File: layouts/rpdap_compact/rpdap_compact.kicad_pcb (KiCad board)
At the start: 4 copper layers, 35.8 x 38.2 mm, 62 parts

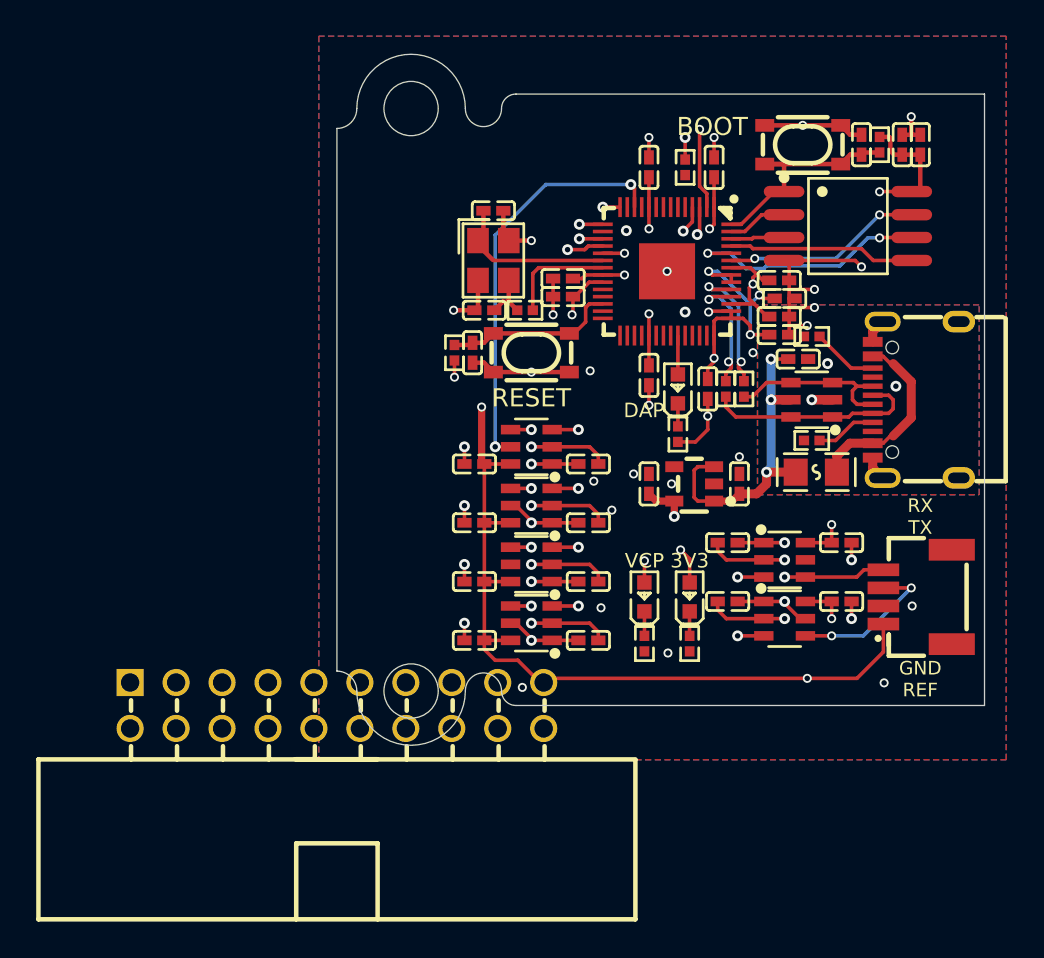
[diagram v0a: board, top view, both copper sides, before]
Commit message: refactor debug-connectors, fix issues in layout and connections
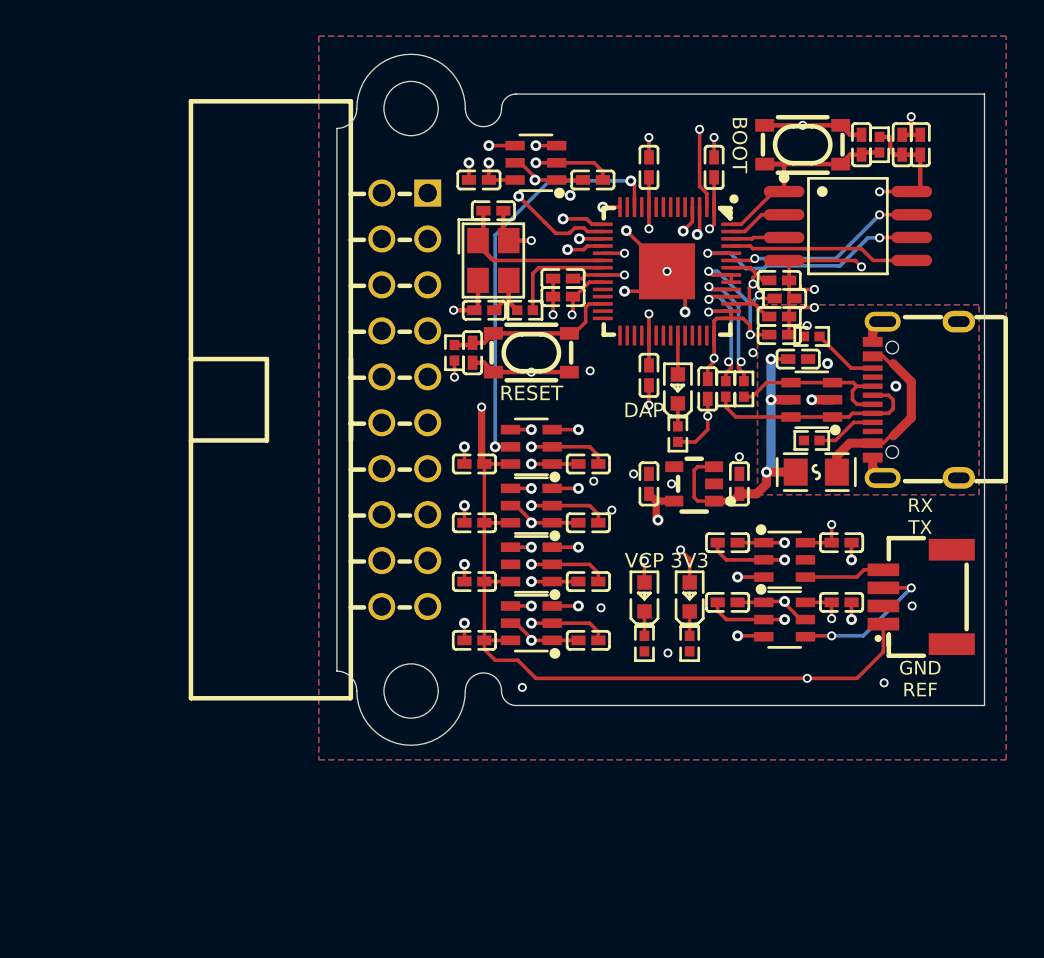
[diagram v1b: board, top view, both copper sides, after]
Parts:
- removed R11: 10kΩ ±1% 62.5mW, UNI_ROYAL_0402WGF1002TCE:R0402
- added C32: 100nF ±10% 16V X7R, Samsung_Electro_Mechanics_CL05B104KO5NNNC:C0402, F.Cu at (21.6, -9.00)
- added C33: 100nF ±10% 16V X7R, Samsung_Electro_Mechanics_CL05B104KO5NNNC:C0402, F.Cu at (27.9, -9.00)
- added U1: , Wuxi_I_core_Elec_AiP74LVC1T45GB236_TR:SOT-23-6_L2.9-W1.6-P0.95-LS2.8-BL, F.Cu at (24.8, -8.05)
- R2: value 100kΩ ±1% 62.5mW -> 10kΩ ±1% 62.5mW; footprint UNI_ROYAL_0402WGF1003TCE:R0402 -> UNI_ROYAL_0402WGF1002TCE:R0402
- moved C12 30.7 mm to (7.85, -29.1), turned to 180 degrees
- moved U7 28.7 mm to (11.0, -30.0), turned to 90 degrees
- moved R2 26.4 mm to (17.0, -3.42), turned to -90 degrees
- moved C11 24.5 mm to (14.2, -29.1), turned to 0 degrees
- moved J1 17.3 mm to (3.75, -16.9), turned to -90 degrees
- moved C14 3.30 mm to (27.9, -5.70)
- moved U8 3.30 mm to (24.8, -4.75)
- moved C13 3.30 mm to (21.6, -5.70)
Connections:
- net DI renamed data_0
- net DO renamed data_1
- net QSPI_SD2 renamed data_2
- net QSPI_SD3 renamed data_3
- net _11 renamed return_test_clock-line
- net _17 renamed DBGRQ
- net _3 renamed N_TRST
- net analog[1]-line renamed gpio[27]-line
- net gpio[11]-line renamed model-a-line-1
- net level_shifter[0]-a-line renamed model-a-line-0
- net level_shifter[2]-a-line renamed model-a-line-2
- net level_shifter[3]-a-line renamed model-a-line-3
- net power_indicator-cathode renamed footprint-cathode-0
- net rpdap-net renamed footprint-net
- net usb_connector-net renamed connector-net
- C1 pad 1: VBUS -> _power_vbus-VCC
- C10 pad 1: 3V3 -> reference-VCC
- C12 pad 1: 3V3 -> reference-VCC
- C14 pad 1: 3V3 -> reference-VCC
- C31 pad 1: VBUS -> _power_vbus-VCC
- C4 pad 1: 3V3 -> reference-VCC
- C6 pad 1: 3V3 -> reference-VCC
- C8 pad 1: 3V3 -> reference-VCC
- CN1 pad 1: 3V3 -> reference-VCC
- CN1 pad 3: TARGET_UART_TX -> uart-TX
- CN1 pad 4: TARGET_UART_RX -> uart-RX
- D1 pad 5: VBUS -> _power_vbus-VCC
- F1 pad 2: VBUS -> _power_vbus-VCC
- J1 pad 1: _1 -> reference-VCC
- J1 pad 10: _10 -> GND
- J1 pad 12: _12 -> GND
- J1 pad 13: _13 -> TDO_SWO
- J1 pad 15: _15 -> nRESET
- J1 pad 19: _19 -> _power_vbus-VCC
- J1 pad 4: _4 -> GND
- J1 pad 5: _5 -> TDI
- J1 pad 6: _6 -> GND
- J1 pad 7: _7 -> TMS_DIO
- J1 pad 8: _8 -> GND
- J1 pad 9: _9 -> TCK_SWCLK
- LED3 pad 1: vcp_indicator-cathode -> footprint-cathode-1
- R2 pad 1: TARGET_GND_DETECT -> footprint-cathode-1
- R2 pad 2: 3V3 -> GND
- U2 pad 1: VBUS -> _power_vbus-VCC
- U2 pad 3: VBUS -> _power_vbus-VCC
- U3 pad 4: TARGET_SWDIO -> TMS_DIO
- U3 pad 6: 3V3 -> reference-VCC
- U4 pad 4: TARGET_SWCLK -> TCK_SWCLK
- U4 pad 5: (no net) -> 3V3
- U4 pad 6: 3V3 -> reference-VCC
- U5 pad 4: TARGET_SWO -> TDO_SWO
- U5 pad 5: GND -> (no net)
- U5 pad 6: 3V3 -> reference-VCC
- U6 pad 4: TARGET_RESET -> nRESET
- U6 pad 5: (no net) -> 3V3
- U6 pad 6: 3V3 -> reference-VCC
- U7 pad 3: TX -> model-a-line-4
- U7 pad 4: TARGET_UART_TX -> TDI
- U7 pad 5: (no net) -> 3V3
- U7 pad 6: 3V3 -> reference-VCC
- U8 pad 3: RX -> a-TX
- U8 pad 4: TARGET_UART_RX -> uart-TX
- U8 pad 5: GND -> 3V3
- U8 pad 6: 3V3 -> reference-VCC
- U9 pad 16: GPIO13 -> model-a-line-4
- U9 pad 2: TX -> a-TX
- U9 pad 3: RX -> a-RX
- U9 pad 5: TARGET_GND_DETECT -> SCL
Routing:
- net (no net): track 135.4 -> 0.00 mm, vias 24 -> 0
- net reference-VCC: track 0.00 -> 77.3 mm, vias 0 -> 5
- net 3V3: track 0.00 -> 66.1 mm, vias 0 -> 20
- net VBUS: track 43.8 -> 0.00 mm, vias 3 -> 0
- net _power_vbus-VCC: track 0.00 -> 43.8 mm, vias 0 -> 3
- net a-TX: track 0.00 -> 37.9 mm, vias 0 -> 2
- net TX: track 37.9 -> 0.00 mm, vias 2 -> 0
- net RX: track 22.9 -> 0.00 mm, vias 2 -> 0
- net a-RX: track 0.00 -> 22.9 mm, vias 0 -> 2
- net GND: track 77.5 -> 91.5 mm, vias 45 -> 49
- net TDI: track 0.00 -> 11.0 mm, vias 0 -> 1
- net TCK_SWCLK: track 0.00 -> 10.7 mm, vias 0 -> 1
- net TARGET_SWCLK: track 10.7 -> 0.00 mm, vias 1 -> 0
- net model-a-line-4: track 0.00 -> 10.4 mm, vias 0 -> 2
- net TMS_DIO: track 0.00 -> 10.2 mm, vias 0 -> 1
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- added copper zone on In1.Cu, net 3V3
- removed copper zone on In1.Cu, net (none)

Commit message: rebuild, small fixes, update README
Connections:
- U1 pad 5: (no net) -> GND
- U5 pad 5: (no net) -> GND
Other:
- outline, holes or cut-outs redrawn
- board text added: "RPDAP"
- board text added: "compact"
- board text added: "{{GITHASH}}"

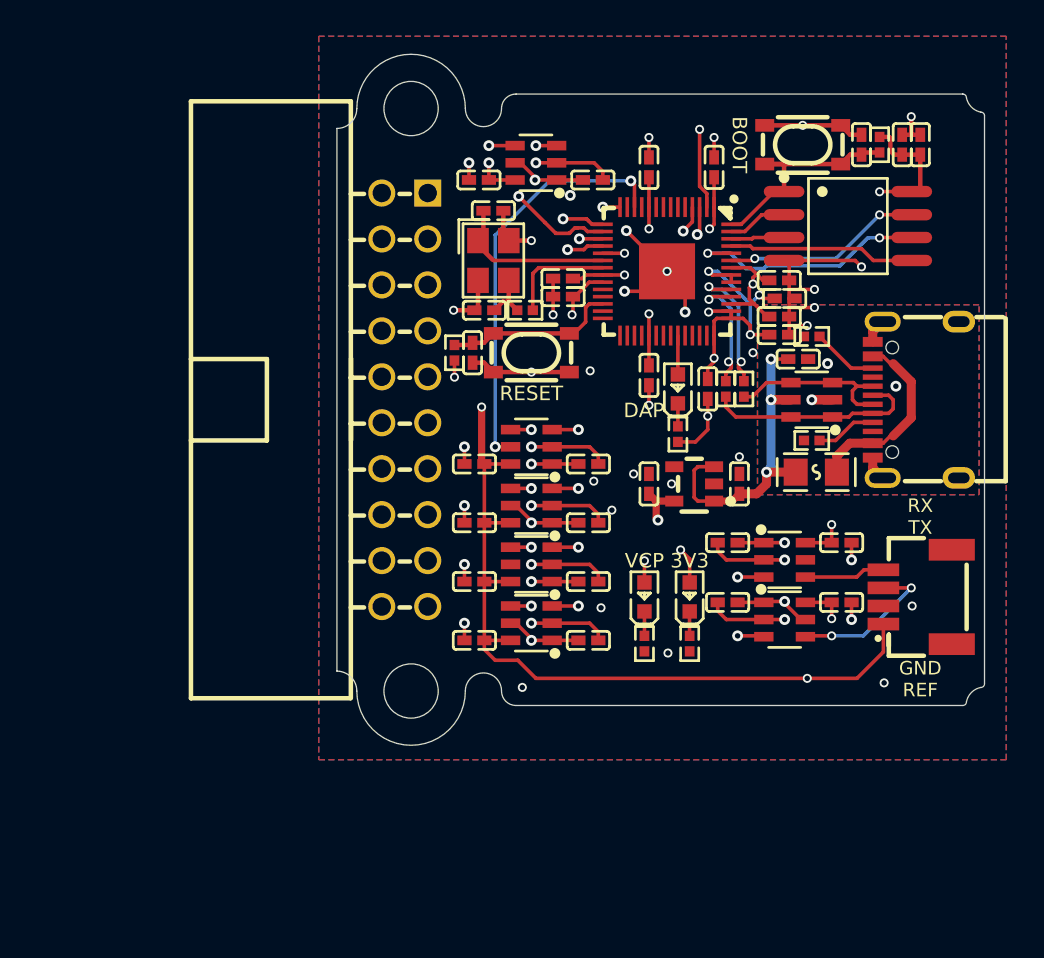
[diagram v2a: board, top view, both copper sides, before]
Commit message: rebuild with upstream rp2040 fixes. move header .25mm to the right. center dap-LED
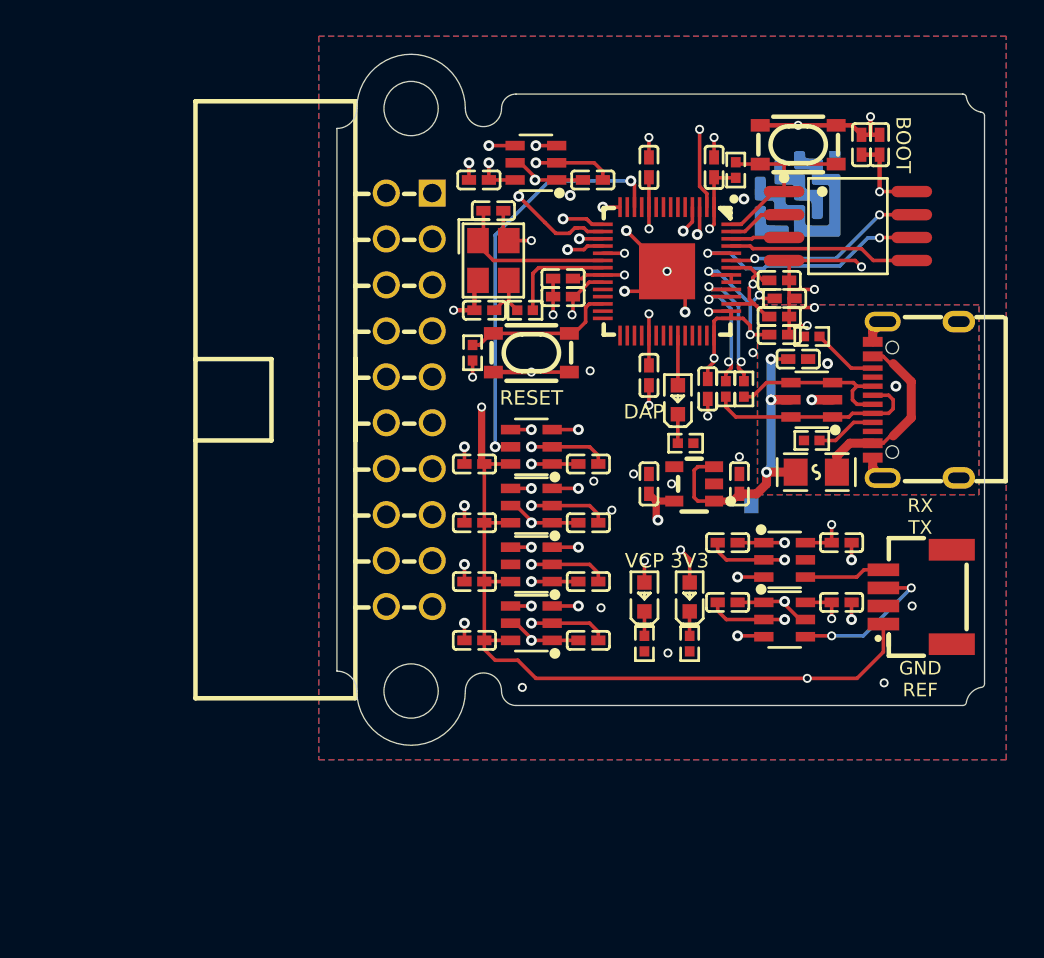
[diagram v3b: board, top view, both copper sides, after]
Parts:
- removed C15, C30: 1µF ±10% 25V X5R, Samsung_Electro_Mechanics_CL05A105KA5NQNC:C0402
- added LOGO1: , atopile_Logo_25x6mm:atopile_Logo_25x6mm, B.Cu at (25.5, -18.0)
- X1: footprint Yangxing_Tech_X322512MSB4SI:CRYSTAL-SMD_4P-L3.2-W2.5-BL -> Abracon_LLC_ABM8_272_T3:CRYSTAL-SMD_4P-L3.2-W2.5-BL
- moved R3 8.07 mm to (22.1, -29.6)
- moved C29 2.25 mm to (29.0, -31.0)
- moved C28 2.25 mm to (30.0, -31.0)
- moved R6 1.00 mm to (7.50, -19.5), turned to -90 degrees
- moved R5 0.66 mm to (19.3, -14.5), turned to 180 degrees
- moved LED2 0.60 mm to (18.9, -16.9)
- moved J1 0.25 mm to (4.00, -16.9)
- moved SW1 0.25 mm to (25.5, -31.0), turned to 180 degrees
- turned SW2 to 0 degrees
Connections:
- net RP_USB_N renamed output-USB_D_N
- net RP_USB_P renamed output-USB_D_P
- net USB_N renamed input-USB_D_N
- net USB_P renamed input-USB_D_P
- net _power_vbus-VCC renamed Vbus_fused
- R3 pad 1: 3V3 -> chip_select
- R3 pad 2: chip_select -> 3V3
- R6 pad 1: 3V3 -> RUN
- R6 pad 2: RUN -> 3V3
- SW1 pad 1: GND -> chip_select
- SW1 pad 2: GND -> chip_select
- SW1 pad 3: chip_select -> GND
- SW1 pad 4: chip_select -> GND
- SW2 pad 1: GND -> RUN
- SW2 pad 2: GND -> RUN
- SW2 pad 3: RUN -> GND
- SW2 pad 4: RUN -> GND
- U1 pad 5: GND -> (no net)
- U5 pad 5: GND -> (no net)
- USB1 pad : connector-net -> (no net)
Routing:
- net GND: track 91.5 -> 87.7 mm, vias 49 -> 50
- net chip_select: track 12.9 -> 10.8 mm
- net RUN: track 9.61 -> 8.61 mm
- net 3V3: track 66.1 -> 65.3 mm
- net A: track 2.15 -> 2.75 mm
- added copper zone on B.Cu, net (none)
- added copper zone on F.Cu, net (none)

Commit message: fix swapped jlink connector pinout + update deps
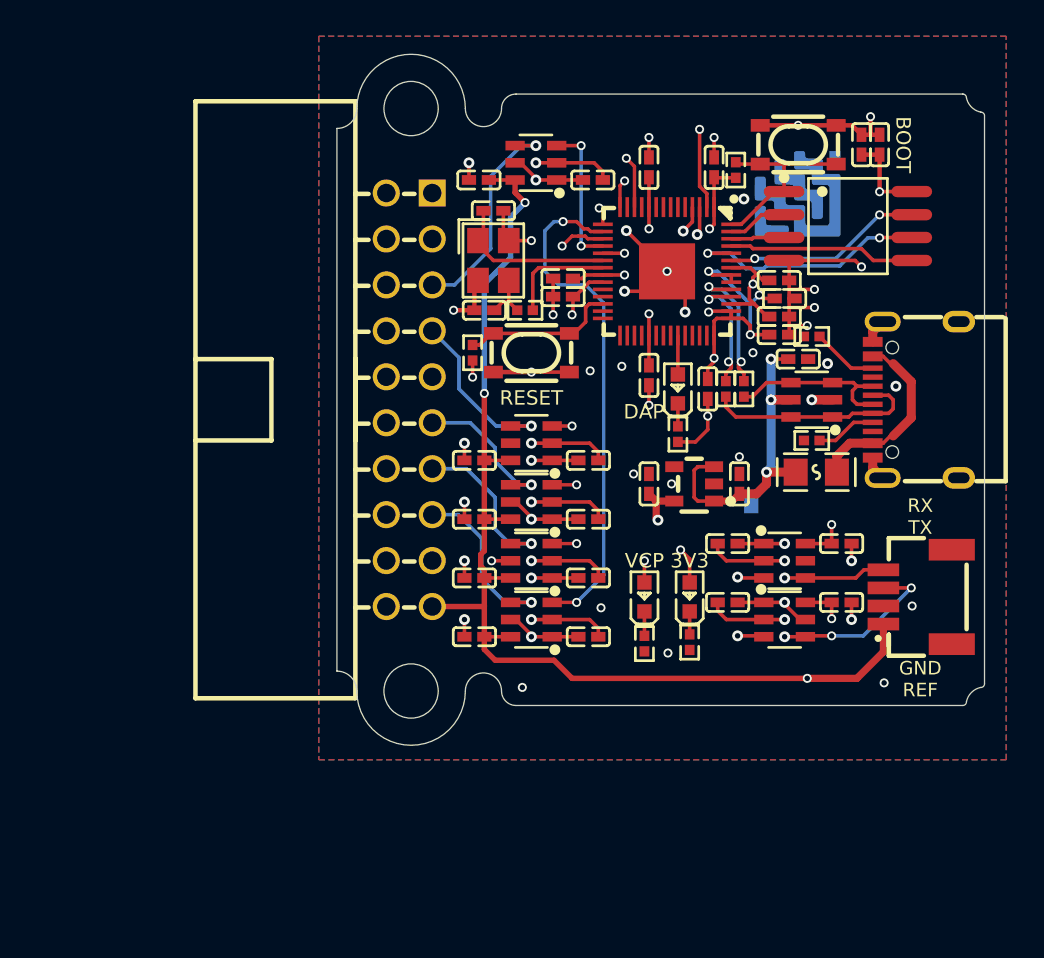
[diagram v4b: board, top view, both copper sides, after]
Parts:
- C16, C21, C28: value 2.2µF ±20% 6.3V X5R -> 2.2µF ±10% 16V X5R; footprint Samsung_Electro_Mechanics_CL05A225MQ5NSNC:C0402 -> Samsung_Electro_Mechanics_CL05A225KO5NQNC:C0402
- LOGO1: moved to F.Cu
- R7, R8: footprint YAGEO_RC0402FR_0727RL:R0402 -> UNI_ROYAL_0402WGF270JTCE:R0402
- moved U7 28.8 mm to (24.8, -4.75), turned to -90 degrees
- moved C10 25.5 mm to (7.85, -29.0)
- moved C9 25.5 mm to (14.1, -29.0)
- moved C11 25.3 mm to (13.9, -3.80)
- moved C12 25.3 mm to (7.60, -3.80)
- moved U5 22.2 mm to (11.0, -30.0)
- moved U1 14.0 mm to (10.8, -8.00), turned to 90 degrees
- moved C8 6.70 mm to (7.60, -13.5)
- moved C7 6.70 mm to (13.9, -13.5)
- moved C3 6.30 mm to (13.9, -7.05)
- moved C4 6.30 mm to (7.60, -7.05)
- moved U4 3.45 mm to (10.8, -14.5)
- moved U8 3.25 mm to (24.8, -8.00)
- moved U3 3.05 mm to (10.8, -11.2)
- moved R5 0.66 mm to (18.9, -15.0), turned to 90 degrees
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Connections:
- net A renamed input-A
- CN1 pad 3: uart-TX -> uart_connector-uart-TX
- CN1 pad 4: uart-RX -> uart_connector-uart-RX
- J1 pad 1: reference-VCC -> Vbus_fused
- J1 pad 11: return_test_clock-line -> TCK_SWCLK
- J1 pad 13: TDO_SWO -> TMS_DIO
- J1 pad 14: _14 -> GND
- J1 pad 15: nRESET -> TDI
- J1 pad 16: _16 -> GND
- J1 pad 17: DBGRQ -> N_TRST
- J1 pad 18: _18 -> GND
- J1 pad 19: Vbus_fused -> reference-VCC
- J1 pad 3: N_TRST -> DBGRQ
- J1 pad 4: GND -> _4
- J1 pad 5: TDI -> nRESET
- J1 pad 6: GND -> _6
- J1 pad 7: TMS_DIO -> TDO_SWO
- J1 pad 8: GND -> _8
- J1 pad 9: TCK_SWCLK -> _9
- U1 pad 3: a-RX -> gpio[12]-A
- U1 pad 4: uart-RX -> TMS_DIO
- U1 pad 5: (no net) -> DIR
- U3 pad 3: model-a-line-0 -> gpio[11]-A
- U3 pad 4: TMS_DIO -> TCK_SWCLK
- U3 pad 5: dir-line -> 3V3
- U4 pad 3: model-a-line-1 -> gpio[14]-A
- U4 pad 4: TCK_SWCLK -> TDO_SWO
- U4 pad 5: 3V3 -> GND
- U5 pad 3: model-a-line-2 -> gpio[15]-A
- U5 pad 4: TDO_SWO -> nRESET
- U5 pad 5: (no net) -> 3V3
- U6 pad 3: model-a-line-3 -> gpio[13]-A
- U6 pad 4: nRESET -> TDI
- U7 pad 3: model-a-line-4 -> mcu-uart-TX
- U7 pad 4: TDI -> uart_connector-uart-TX
- U8 pad 3: a-TX -> mcu-uart-RX
- U8 pad 4: uart-TX -> uart_connector-uart-RX
- U8 pad 5: 3V3 -> GND
- U9 pad 12: dir-line -> DIR
- U9 pad 14: model-a-line-1 -> gpio[11]-A
- U9 pad 15: model-a-line-0 -> gpio[12]-A
- U9 pad 16: model-a-line-4 -> gpio[13]-A
- U9 pad 17: model-a-line-2 -> gpio[14]-A
- U9 pad 18: model-a-line-3 -> gpio[15]-A
- U9 pad 2: a-TX -> mcu-uart-TX
- U9 pad 3: a-RX -> mcu-uart-RX
- USB1 pad : (no net) -> connector-net
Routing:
- net mcu-uart-TX: track 0.00 -> 37.9 mm, vias 0 -> 2
- net a-TX: track 37.9 -> 0.00 mm, vias 2 -> 0
- net DIR: track 0.00 -> 34.5 mm, vias 0 -> 2
- net gpio[13]-A: track 0.00 -> 28.4 mm, vias 0 -> 2
- net model-a-line-3: track 26.1 -> 0.00 mm, vias 2 -> 0
- net model-a-line-1: track 23.6 -> 0.00 mm, vias 2 -> 0
- net mcu-uart-RX: track 0.00 -> 22.9 mm, vias 0 -> 2
- net a-RX: track 22.9 -> 0.00 mm, vias 2 -> 0
- net dir-line: track 22.8 -> 0.00 mm, vias 2 -> 0
- net gpio[12]-A: track 0.00 -> 22.5 mm, vias 0 -> 2
- net model-a-line-2: track 22.3 -> 0.00 mm, vias 2 -> 0
- net gpio[11]-A: track 0.00 -> 20.8 mm, vias 0 -> 2
- net model-a-line-0: track 17.2 -> 0.00 mm, vias 2 -> 0
- net gpio[14]-A: track 0.00 -> 14.7 mm, vias 0 -> 2
- net model-a-line-4: track 10.4 -> 0.00 mm, vias 2 -> 0
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- removed copper zone on B.Cu, net (none)
- removed copper zone on F.Cu, net (none)
